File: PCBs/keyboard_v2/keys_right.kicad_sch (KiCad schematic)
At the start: 55 parts, among them SW701 RIC11-31S15.5D7-TH, SW702 SW_DIP_x01, SW703 SW_DIP_x01, SW704 SW_DIP_x01, SW705 SW_DIP_x01, SW706 SW_DIP_x01, SW707 SW_DIP_x01, SW708 SW_DIP_x01, SW709 SW_DIP_x01, SW710 SW_DIP_x01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

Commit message: V2 progress
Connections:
- net KEY_E4: now also SW712.2; no longer SW702.2
- net KEY_E6: now also SW702.2; no longer SW712.2
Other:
- moved on the sheet: SW702, SW707, SW712

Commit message: Display schematic done
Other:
- note added: "Level shifter"
- note added: "encoder should probably use 3v3"
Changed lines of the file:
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@@
 	(wire
 		(pts
-			(xy 22.86 38.1) (xy 27.94 38.1)
+			(xy 17.78 38.1) (xy 27.94 38.1)
 		)
 		(stroke
@@
 		)
 	)
+	(text "encoder should probably use 3v3"
+		(exclude_from_sim no)
+		(at 195.58 170.18 0)
+		(effects
+			(font
+				(size 1.27 1.27)
+			)
+		)
+	)
+	(text "Level shifter"
+		(exclude_from_sim no)
+		(at 40.64 101.6 0)
+		(effects
+			(font
+				(size 1.27 1.27)
+			)
+		)
+	)
 	(label "LED10"
 		(at 281.94 38.1 180)
@@
 		)
 	)
+	(label "LED1"
+		(at 17.78 38.1 0)
+		(fields_autoplaced yes)
+		(effects
+			(font
+				(size 1.27 1.27)
+			)
+			(justify left bottom)
+		)
+	)
 	(label "LED6"
 		(at 160.02 38.1 0)
@@
 		)
 	)
+	(label "LED1"
+		(at 48.26 101.6 0)
+		(fields_autoplaced yes)
+		(effects
+			(font
+				(size 1.27 1.27)
+			)
+			(justify left bottom)
+		)
+	)
 	(label "LED26"
 		(at 215.9 68.58 0)
@@
 		)
 	)
-	(hierarchical_label "LED1"
-		(shape input)
-		(at 22.86 38.1 180)
-		(fields_autoplaced yes)
-		(effects
-			(font
-				(size 1.27 1.27)
-			)
-			(justify right)
-		)
-	)
 	(hierarchical_label "KEY_D12"
 		(shape output)
@@
 		)
 	)
+	(hierarchical_label "NEOPIXEL"
+		(shape input)
+		(at 33.02 101.6 180)
+		(fields_autoplaced yes)
+		(effects
+			(font
+				(size 1.27 1.27)
+			)
+			(justify right)
+		)
+	)
 	(hierarchical_label "ENC_B"
 		(shape output)
@@
 					(unit 1)
 				)
+			)
+		)
+	)
+	(symbol
+		(lib_id "power:VBUS")
+		(at 40.64 96.52 0)
+		(unit 1)
+		(exclude_from_sim no)
+		(in_bom yes)
+		(on_board yes)
+		(dnp no)
+		(fields_autoplaced yes)
+		(property "Reference" "#PWR0730"
+			(at 40.64 100.33 0)
+			(effects
+				(font
+					(size 1.27 1.27)
+				)
+				(hide yes)
+			)
+		)
+		(property "Value" "VBUS"
+			(at 40.64 91.44 0)
+			(effects
+				(font
+					(size 1.27 1.27)
+				)
+			)
+		)
+		(property "Footprint" ""
+			(at 40.64 96.52 0)
+			(effects
+				(font
+					(size 1.27 1.27)
+				)
+				(hide yes)
+			)
+		)
+		(property "Datasheet" ""
+			(at 40.64 96.52 0)
+			(effects
+				(font
+					(size 1.27 1.27)
+				)
+				(hide yes)
+			)
+		)
+		(property "Description" "Power symbol creates a global label with name \"VBUS\""
+			(at 40.64 96.52 0)
+			(effects
+				(font
+					(size 1.27 1.27)
+				)
+				(hide yes)
+			)
+		)
+		(pin "1"
+		)
+		(instances
+			(project "keyboard_v2"
+				(path "/e2360b7f-be71-48d9-b398-9f8cd45479d6/b599252a-0e44-4760-9c79-385d4380db60/71cccd57-3bdf-4b46-98ad-b3032f34eaad"
+					(reference "#PWR0730")
+					(unit 1)
+				)

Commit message: V2 Schematic mostly done
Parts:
- added Q701: DMN21D2UFB-7B, keyboard_footprints:DMN21D2UFB7B, symbol DMN21D2UFB-7B:DMN21D2UFB-7B
- added R701: 4k7, Resistor_SMD:R_0402_1005Metric, symbol Device:R_Small
- added R708, R709: 100k, Resistor_SMD:R_0402_1005Metric, symbol Device:R_Small
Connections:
- net ENC_A: now also R708.2; no longer SW701.A
- net ENC_B: now also SW701.A, R709.2
- net LED1: now also Q701.3 (D), R701.2
- net NEOPIXEL: now also Q701.2 (S)
- net VBUS: now also R701.1
- new net +1V8: Q701.1 (G)
- new net +VSYS: R708.1, R709.1
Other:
- note removed: "Level shifter"
- note removed: "encoder should probably use 3v3"
- moved on the sheet: D701, D702, D703, D704, D705, D706, D707, D708, D709, D710, D711, D712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

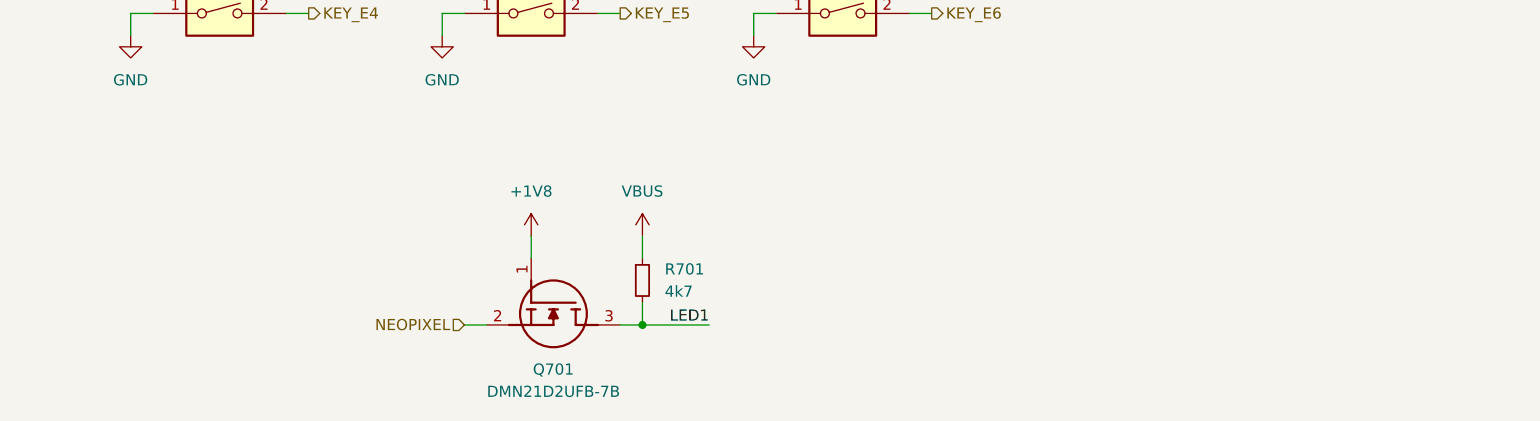
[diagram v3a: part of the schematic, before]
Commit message: Schematic mostly done, moving onto PCB
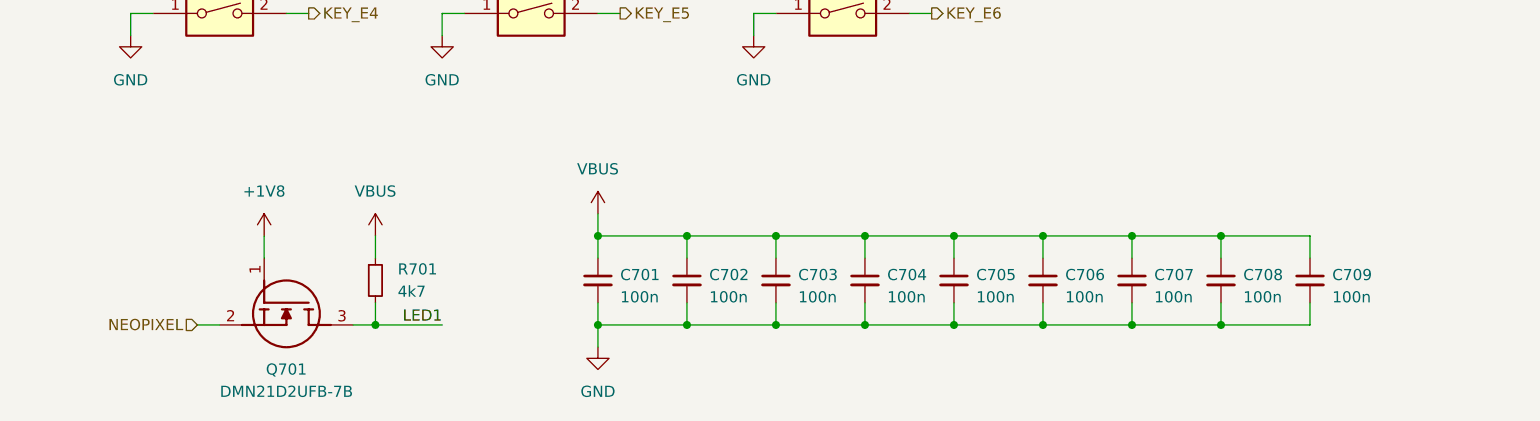
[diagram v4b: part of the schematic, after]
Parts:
- added C701, C702, C703, C704, C705, C706, C707, C708, C709: 100n, Capacitor_SMD:C_0402_1005Metric, symbol Device:C_Small
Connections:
- net GND: now also C701.2, C702.2, C703.2, C704.2, C705.2, C706.2, C707.2, C708.2, C709.2
- net VBUS: now also C701.1, C702.1, C703.1, C704.1, C705.1, C706.1, C707.1, C708.1, C709.1
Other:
- moved on the sheet: Q701, R701
